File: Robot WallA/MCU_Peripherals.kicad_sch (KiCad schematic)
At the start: 44 parts, among them IC3 LAN8742A-CZ-TR, IC4 USBLC6-4SC6, IC6 USBLC6-4SC6, J3 USB4216-03-A, J6 SS-90000-009, T1 H1102NL

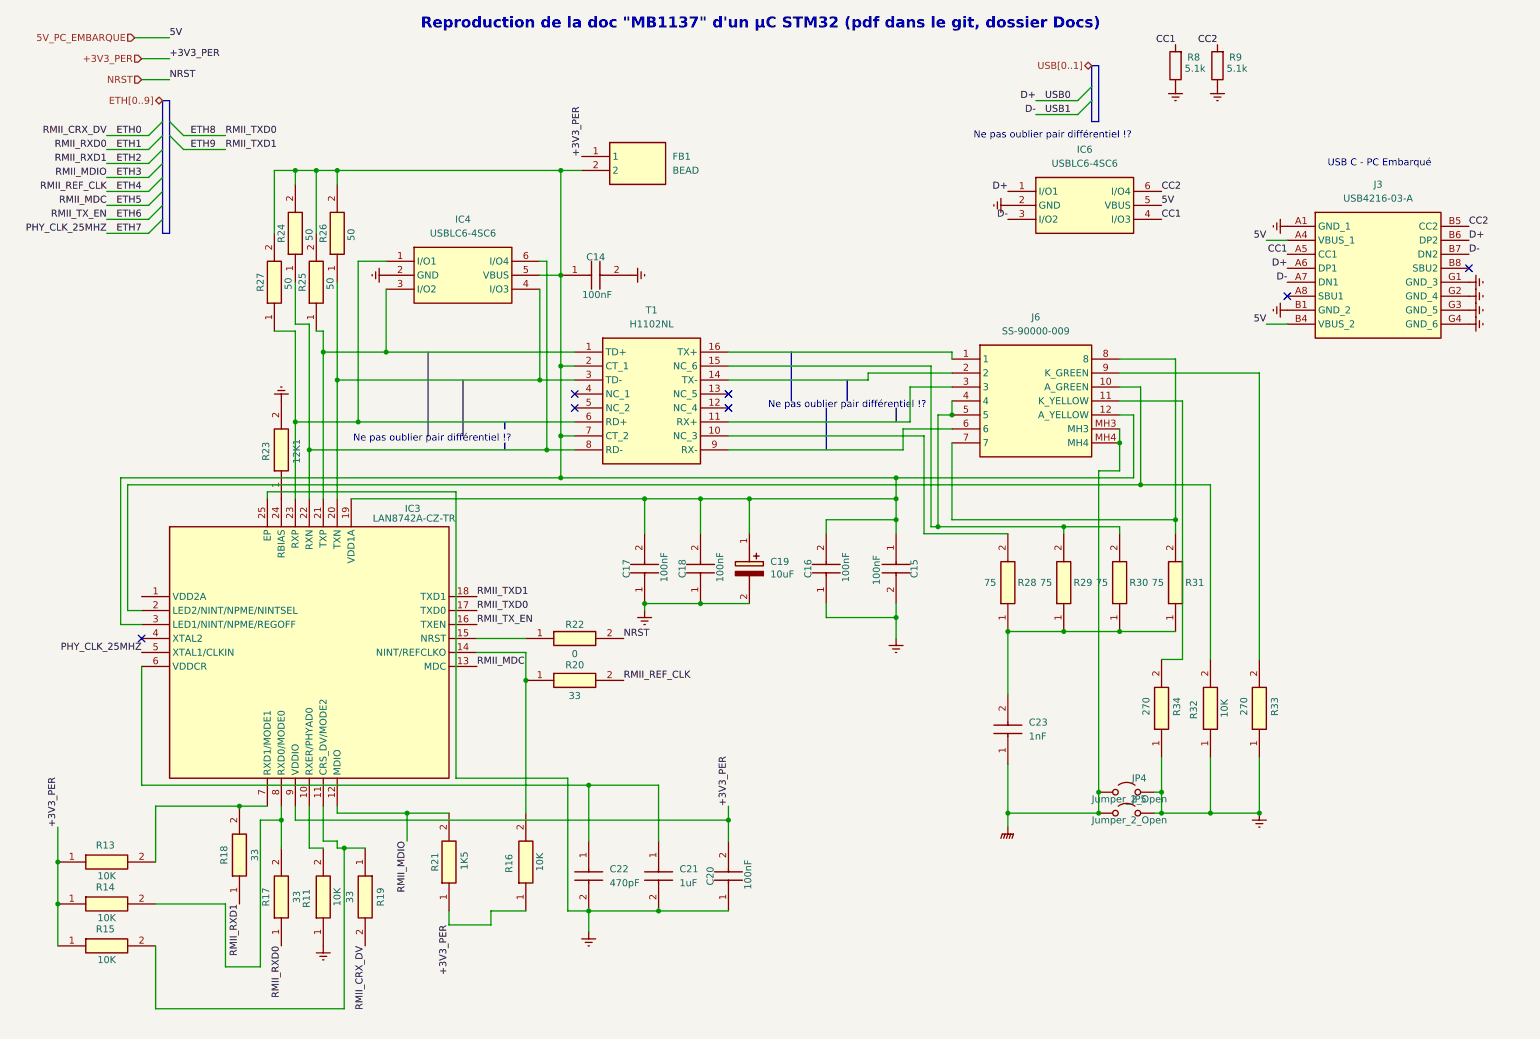
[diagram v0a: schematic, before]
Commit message: Continued to link MCU pins, Added a sheet for servomotors and optional 2 DC motors.
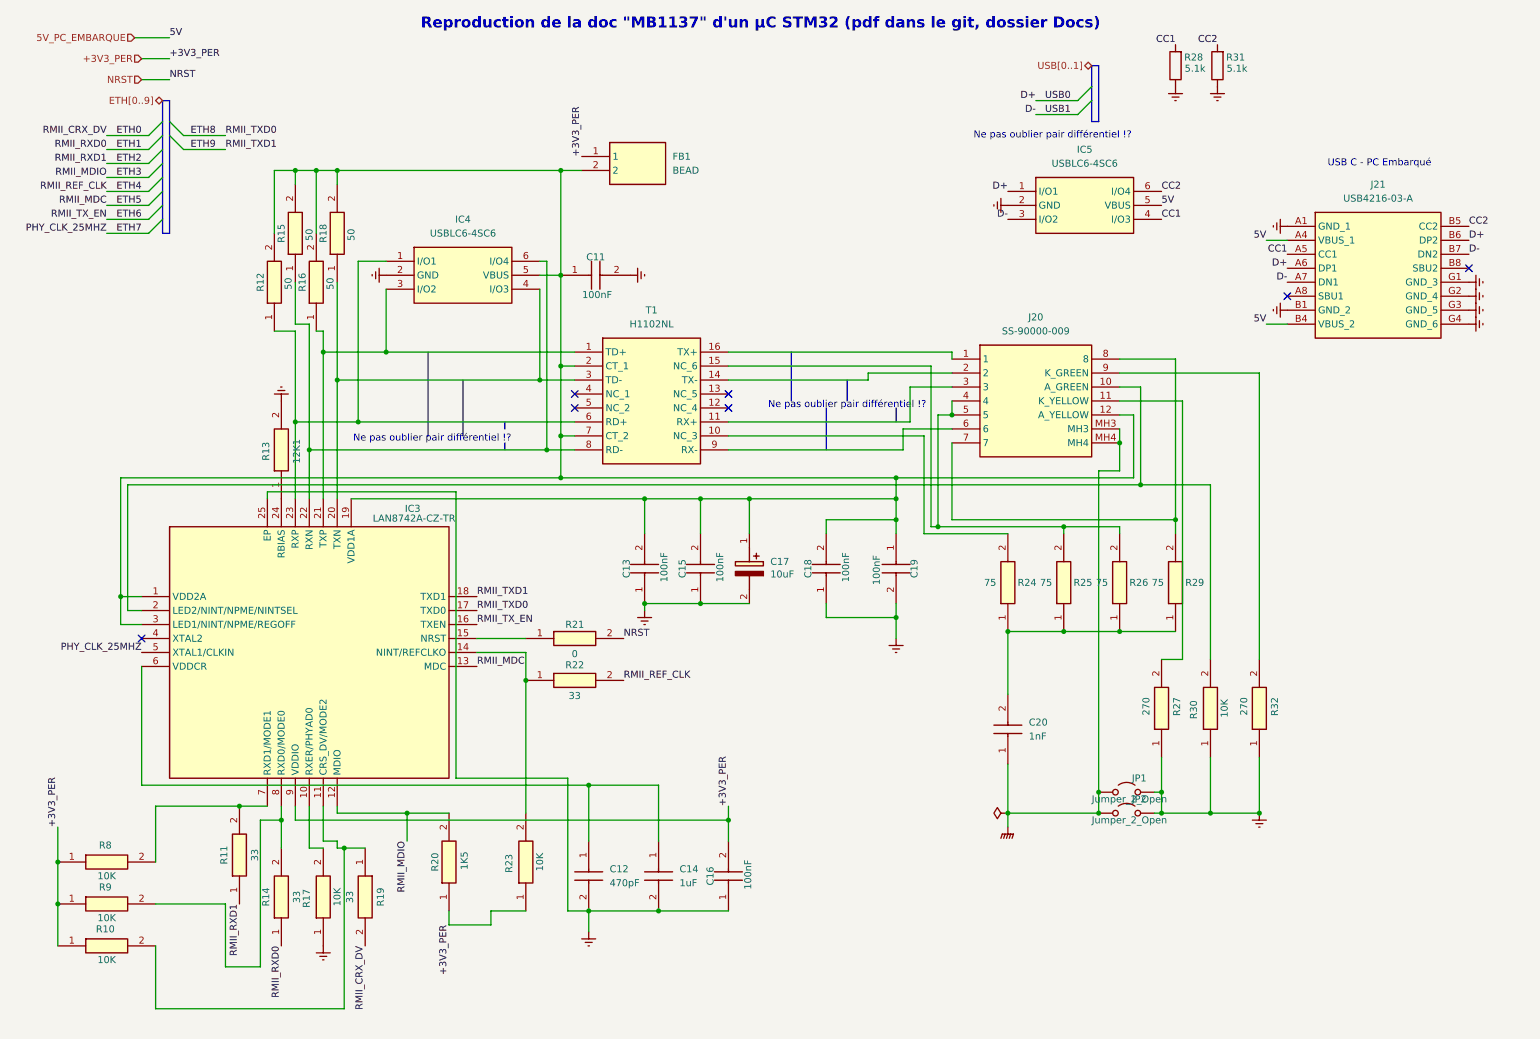
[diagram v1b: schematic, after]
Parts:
- renumbered C14 to C11, C22 to C12, C17 to C13, C21 to C14, C18 to C15, C20 to C16, C19 to C17, C16 to C18, C15 to C19, C23 to C20, IC6 to IC5, J6 to J20, J3 to J21, JP4 to JP1, JP5 to JP2, R15 to R10, R18 to R11, R27 to R12, R23 to R13, R17 to R14, R24 to R15, R25 to R16, R11 to R17, R26 to R18, R21 to R20, R22 to R21, R20 to R22, R16 to R23, R28 to R24, R29 to R25, R30 to R26, R34 to R27, R8 to R28, R31 to R29, R32 to R30, R9 to R31, R33 to R32, R13 to R8, R14 to R9
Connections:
- net at C11.1, C13.2, C15.2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: now also IC3.1 (VDD2A)

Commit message: Defined every footprints
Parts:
- C23: renamed from C11; footprint CAPC1608X90N -> Capacitor_SMD:C_0603_1608Metric_Pad1.08x0.95mm_HandSolder; Arrow Part Number CC0603KRX7R7BB104 -> (none); Arrow Price/Stock https://www.arrow.com/en/products/cc0603krx7r7bb104/yageo?u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 -> (none); Height 0.9 -> (none); Manufacturer_Name YAGEO -> (none); Manufacturer_Part_Number CC0603KRX7R7BB104 -> (none); Mouser Part Number 603-CC603KRX7R7BB104 -> (none); Mouser Price/Stock https://www.mouser.co.uk/ProductDetail/YAGEO/CC0603KRX7R7BB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 -> (none)
- C24: renamed from C17; footprint CAPPM3216X180N -> Capacitor_SMD:C_0603_1608Metric_Pad1.08x0.95mm_HandSolder; Height 1.8 -> (none); Manufacturer_Name Kyocera AVX -> (none); Manufacturer_Part_Number TAJA106K016R -> (none); Mouser Part Number N/A -> (none); Mouser Price/Stock https://www.mouser.co.uk/ProductDetail/KYOCERA-AVX/TAJA106K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 -> (none)
- C25: renamed from C19; footprint CAPC1608X90N -> Capacitor_SMD:C_0603_1608Metric_Pad1.08x0.95mm_HandSolder; Arrow Part Number CC0603KRX7R7BB104 -> (none); Arrow Price/Stock https://www.arrow.com/en/products/cc0603krx7r7bb104/yageo?u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 -> (none); Height 0.9 -> (none); Manufacturer_Name YAGEO -> (none); Manufacturer_Part_Number CC0603KRX7R7BB104 -> (none); Mouser Part Number 603-CC603KRX7R7BB104 -> (none); Mouser Price/Stock https://www.mouser.co.uk/ProductDetail/YAGEO/CC0603KRX7R7BB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 -> (none)
- C26: renamed from C13; footprint CAPC1608X90N -> Capacitor_SMD:C_0603_1608Metric_Pad1.08x0.95mm_HandSolder; Arrow Part Number CC0603KRX7R7BB104 -> (none); Arrow Price/Stock https://www.arrow.com/en/products/cc0603krx7r7bb104/yageo?u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 -> (none); Height 0.9 -> (none); Manufacturer_Name YAGEO -> (none); Manufacturer_Part_Number CC0603KRX7R7BB104 -> (none); Mouser Part Number 603-CC603KRX7R7BB104 -> (none); Mouser Price/Stock https://www.mouser.co.uk/ProductDetail/YAGEO/CC0603KRX7R7BB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 -> (none)
- C27: renamed from C15; footprint CAPC1608X90N -> Capacitor_SMD:C_0603_1608Metric_Pad1.08x0.95mm_HandSolder; Arrow Part Number CC0603KRX7R7BB104 -> (none); Arrow Price/Stock https://www.arrow.com/en/products/cc0603krx7r7bb104/yageo?u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 -> (none); Height 0.9 -> (none); Manufacturer_Name YAGEO -> (none); Manufacturer_Part_Number CC0603KRX7R7BB104 -> (none); Mouser Part Number 603-CC603KRX7R7BB104 -> (none); Mouser Price/Stock https://www.mouser.co.uk/ProductDetail/YAGEO/CC0603KRX7R7BB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 -> (none)
- C28: renamed from C18; footprint CAPC1608X90N -> Capacitor_SMD:C_0603_1608Metric_Pad1.08x0.95mm_HandSolder; Arrow Part Number CC0603KRX7R7BB104 -> (none); Arrow Price/Stock https://www.arrow.com/en/products/cc0603krx7r7bb104/yageo?u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 -> (none); Height 0.9 -> (none); Manufacturer_Name YAGEO -> (none); Manufacturer_Part_Number CC0603KRX7R7BB104 -> (none); Mouser Part Number 603-CC603KRX7R7BB104 -> (none); Mouser Price/Stock https://www.mouser.co.uk/ProductDetail/YAGEO/CC0603KRX7R7BB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 -> (none)
- C29: renamed from C20; footprint CAPC3216X145N -> Capacitor_SMD:C_0603_1608Metric_Pad1.08x0.95mm_HandSolder; Arrow Part Number CC1206KKX7RDBB102 -> (none); Arrow Price/Stock https://www.arrow.com/en/products/cc1206kkx7rdbb102/yageo?u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 -> (none); Height 1.45 -> (none); Manufacturer_Name YAGEO -> (none); Manufacturer_Part_Number CC1206KKX7RDBB102 -> (none); Mouser Part Number 603-CC206KKX7RDBB102 -> (none); Mouser Price/Stock https://www.mouser.co.uk/ProductDetail/YAGEO/CC1206KKX7RDBB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 -> (none)
- C30: renamed from C12; footprint CAPC1608X90N -> Capacitor_SMD:C_0603_1608Metric_Pad1.08x0.95mm_HandSolder; Height 0.9 -> (none); Manufacturer_Name YAGEO -> (none); Manufacturer_Part_Number CC0603JRNPO9BN471 -> (none); Mouser Part Number 603-C0603JRNPO9BN471 -> (none); Mouser Price/Stock https://www.mouser.co.uk/ProductDetail/YAGEO/CC0603JRNPO9BN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 -> (none)
- C31: renamed from C14; footprint CAPC1608X90N -> Capacitor_SMD:C_0603_1608Metric_Pad1.08x0.95mm_HandSolder; Arrow Part Number CC0603KRX5R7BB105 -> (none); Arrow Price/Stock https://www.arrow.com/en/products/cc0603krx5r7bb105/yageo?u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 -> (none); Height 0.9 -> (none); Manufacturer_Name YAGEO -> (none); Manufacturer_Part_Number CC0603KRX5R7BB105 -> (none); Mouser Part Number 603-CC603KRX5R7BB105 -> (none); Mouser Price/Stock https://www.mouser.co.uk/ProductDetail/YAGEO/CC0603KRX5R7BB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 -> (none)
- C32: renamed from C16; footprint CAPC1608X90N -> Capacitor_SMD:C_0603_1608Metric_Pad1.08x0.95mm_HandSolder; Arrow Part Number CC0603KRX7R7BB104 -> (none); Arrow Price/Stock https://www.arrow.com/en/products/cc0603krx7r7bb104/yageo?u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 -> (none); Height 0.9 -> (none); Manufacturer_Name YAGEO -> (none); Manufacturer_Part_Number CC0603KRX7R7BB104 -> (none); Mouser Part Number 603-CC603KRX7R7BB104 -> (none); Mouser Price/Stock https://www.mouser.co.uk/ProductDetail/YAGEO/CC0603KRX7R7BB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 -> (none)
- FB2: renamed from FB1; value BEAD -> Bead 600R; footprint BEADC1608X95N -> Resistor_SMD:R_0603_1608Metric_Pad0.98x0.95mm_HandSolder; Height 0.95 -> (none); Manufacturer_Name TAITEC -> (none); Manufacturer_Part_Number FCM1608KF-601T05 -> FCM 1608KF-601T03
- IC3: renamed from IC5; footprint SOT95P280X145-6N -> SamacSys_Parts:SOT95P280X145-6N; Arrow Part Number USBLC6-4SC6 -> (none); Arrow Price/Stock https://www.arrow.com/en/products/usblc6-4sc6/stmicroelectr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 -> (none); Height 1.45 -> (none); Manufacturer_Name STMicroelectronics -> (none); Mouser Part Number 511-USBLC6-4SC6 -> (none); Mouser Price/Stock https://www.mouser.co.uk/ProductDetail/STMicroelectronics/U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 -> (none)
- IC4: footprint SOT95P280X145-6N -> SamacSys_Parts:SOT95P280X145-6N; Arrow Part Number USBLC6-4SC6 -> (none); Arrow Price/Stock https://www.arrow.com/en/products/usblc6-4sc6/stmicroelectr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 -> (none); Height 1.45 -> (none); Manufacturer_Name STMicroelectronics -> (none); Mouser Part Number 511-USBLC6-4SC6 -> (none); Mouser Price/Stock https://www.mouser.co.uk/ProductDetail/STMicroelectronics/U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 -> (none)
- IC5: renamed from IC3; footprint QFN50P400X400X100-25N-D -> SamacSys_Parts:QFN50P400X400X100-25N-D; Arrow Part Number LAN8742A-CZ-TR -> (none); Arrow Price/Stock https://www.arrow.com/en/products/lan8742a-cz-tr/microchip-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 -> (none); Height 1 -> (none); Manufacturer_Name Microchip -> (none); Mouser Part Number 579-LAN8742A-CZ-TR -> (none); Mouser Price/Stock https://www.mouser.co.uk/ProductDetail/Microchip-Technology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 -> (none)
- J2: renamed from J21; footprint USB421603A -> SamacSys_Parts:USB421603A; Manufacturer_Name GCT (GLOBAL CONNECTOR TECHNOLOGY) -> (none); Mouser Part Number 640-USB4216-03-A -> (none); Mouser Price/Stock https://www.mouser.co.uk/ProductDetail/GCT/USB4216-03-A?qs=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 -> (none)
- J3: renamed from J20; footprint SS90000009 -> SamacSys_Parts:SS90000009; Height 13.38 -> (none); Manufacturer_Name Bel -> (none)
- JP4: renamed from JP1; value Jumper_2_Open -> SolderJumper; footprint (none) -> Jumper:SolderJumper-2_P1.3mm_Open_Pad1.0x1.5mm; now left out of the parts list
- JP5: renamed from JP2; value Jumper_2_Open -> SolderJumper; footprint (none) -> Jumper:SolderJumper-2_P1.3mm_Open_Pad1.0x1.5mm; now left out of the parts list
- R10: renamed from R25; value 75 -> 75R; footprint RESC1608X55N -> Resistor_SMD:R_0603_1608Metric_Pad0.98x0.95mm_HandSolder; Arrow Part Number RC0603FR-0775RL -> (none); Arrow Price/Stock https://www.arrow.com/en/products/rc0603fr-0775rl/yageo?reg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 -> (none); Height 0.55 -> (none); Manufacturer_Name KEMET -> (none); Manufacturer_Part_Number RC0603FR-0775RL -> (none); Mouser Part Number 603-RC0603FR-0775RL -> (none); Mouser Price/Stock https://www.mouser.co.uk/ProductDetail/YAGEO/RC0603FR-0775R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 -> (none)
- R11: renamed from R26; value 75 -> 75R; footprint RESC1608X55N -> Resistor_SMD:R_0603_1608Metric_Pad0.98x0.95mm_HandSolder; Arrow Part Number RC0603FR-0775RL -> (none); Arrow Price/Stock https://www.arrow.com/en/products/rc0603fr-0775rl/yageo?reg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 -> (none); Height 0.55 -> (none); Manufacturer_Name KEMET -> (none); Manufacturer_Part_Number RC0603FR-0775RL -> (none); Mouser Part Number 603-RC0603FR-0775RL -> (none); Mouser Price/Stock https://www.mouser.co.uk/ProductDetail/YAGEO/RC0603FR-0775R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 -> (none)
- R12: renamed from R29; value 75 -> 75R; footprint RESC1608X55N -> Resistor_SMD:R_0603_1608Metric_Pad0.98x0.95mm_HandSolder; Arrow Part Number RC0603FR-0775RL -> (none); Arrow Price/Stock https://www.arrow.com/en/products/rc0603fr-0775rl/yageo?reg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 -> (none); Height 0.55 -> (none); Manufacturer_Name KEMET -> (none); Manufacturer_Part_Number RC0603FR-0775RL -> (none); Mouser Part Number 603-RC0603FR-0775RL -> (none); Mouser Price/Stock https://www.mouser.co.uk/ProductDetail/YAGEO/RC0603FR-0775R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 -> (none)
- R13: renamed from R21; value 0 -> 0R; footprint RESC1608X50N -> Resistor_SMD:R_0603_1608Metric_Pad0.98x0.95mm_HandSolder; Arrow Part Number CRCW06030000Z0EI -> (none); Arrow Price/Stock https://www.arrow.com/en/products/crcw06030000z0ei/vishay?u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 -> (none); Height 0.5 -> (none); Manufacturer_Name Vishay -> (none); Manufacturer_Part_Number CRCW06030000Z0EI -> (none); Mouser Part Number 71-CRCW06030000Z0EI -> (none); Mouser Price/Stock https://www.mouser.co.uk/ProductDetail/Vishay-Dale/CRCW0603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 -> (none)
- R14: renamed from R22; value 33 -> 33R; footprint RESC1608X55N -> Resistor_SMD:R_0603_1608Metric_Pad0.98x0.95mm_HandSolder; Height 0.55 -> (none); Manufacturer_Name TE Connectivity -> (none); Manufacturer_Part_Number CRG0603F33R -> (none); Mouser Part Number 279-CRG0603F33R -> (none); Mouser Price/Stock https://www.mouser.co.uk/ProductDetail/TE-Connectivity-Hols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 -> (none)
- R15: renamed from R27; value 270 -> 270R; footprint RESC1608X55N -> Resistor_SMD:R_0603_1608Metric_Pad0.98x0.95mm_HandSolder; Arrow Part Number RC0603FR-07270RL -> (none); Arrow Price/Stock https://www.arrow.com/en/products/rc0603fr-07270rl/yageo?re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 -> (none); Height 0.55 -> (none); Manufacturer_Name KEMET -> (none); Manufacturer_Part_Number RC0603FR-07270RL -> (none); Mouser Part Number 603-RC0603FR-07270RL -> (none); Mouser Price/Stock https://www.mouser.co.uk/ProductDetail/Yageo/RC0603FR-07270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 -> (none)
- R16: renamed from R30; footprint RESC1608X50N -> Resistor_SMD:R_0603_1608Metric_Pad0.98x0.95mm_HandSolder; Arrow Part Number CRCW060310K0FKEI -> (none); Arrow Price/Stock https://www.arrow.com/en/products/crcw060310k0fkei/vishay?u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 -> (none); Height 0.5 -> (none); Manufacturer_Name Vishay -> (none); Manufacturer_Part_Number CRCW060310K0FKEI -> (none); Mouser Part Number 71-CRCW060310K0FKEI -> (none); Mouser Price/Stock https://www.mouser.co.uk/ProductDetail/Vishay-Dale/CRCW0603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 -> (none)
- R17: renamed from R32; value 270 -> 270R; footprint RESC1608X55N -> Resistor_SMD:R_0603_1608Metric_Pad0.98x0.95mm_HandSolder; Arrow Part Number RC0603FR-07270RL -> (none); Arrow Price/Stock https://www.arrow.com/en/products/rc0603fr-07270rl/yageo?re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 -> (none); Height 0.55 -> (none); Manufacturer_Name KEMET -> (none); Manufacturer_Part_Number RC0603FR-07270RL -> (none); Mouser Part Number 603-RC0603FR-07270RL -> (none); Mouser Price/Stock https://www.mouser.co.uk/ProductDetail/Yageo/RC0603FR-07270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 -> (none)
- R18: renamed from R19; value 33 -> 33R; footprint RESC1608X55N -> Resistor_SMD:R_0603_1608Metric_Pad0.98x0.95mm_HandSolder; Height 0.55 -> (none); Manufacturer_Name TE Connectivity -> (none); Manufacturer_Part_Number CRG0603F33R -> (none); Mouser Part Number 279-CRG0603F33R -> (none); Mouser Price/Stock https://www.mouser.co.uk/ProductDetail/TE-Connectivity-Hols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 -> (none)
- R19: renamed from R8; footprint RESC1608X50N -> Resistor_SMD:R_0603_1608Metric_Pad0.98x0.95mm_HandSolder; Arrow Part Number CRCW060310K0FKEI -> (none); Arrow Price/Stock https://www.arrow.com/en/products/crcw060310k0fkei/vishay?u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 -> (none); Height 0.5 -> (none); Manufacturer_Name Vishay -> (none); Manufacturer_Part_Number CRCW060310K0FKEI -> (none); Mouser Part Number 71-CRCW060310K0FKEI -> (none); Mouser Price/Stock https://www.mouser.co.uk/ProductDetail/Vishay-Dale/CRCW0603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 -> (none)
- R2: renamed from R28; footprint (none) -> Resistor_SMD:R_0603_1608Metric_Pad0.98x0.95mm_HandSolder
- R20: renamed from R9; footprint RESC1608X50N -> Resistor_SMD:R_0603_1608Metric_Pad0.98x0.95mm_HandSolder; Arrow Part Number CRCW060310K0FKEI -> (none); Arrow Price/Stock https://www.arrow.com/en/products/crcw060310k0fkei/vishay?u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 -> (none); Height 0.5 -> (none); Manufacturer_Name Vishay -> (none); Manufacturer_Part_Number CRCW060310K0FKEI -> (none); Mouser Part Number 71-CRCW060310K0FKEI -> (none); Mouser Price/Stock https://www.mouser.co.uk/ProductDetail/Vishay-Dale/CRCW0603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 -> (none)
- R21: renamed from R11; value 33 -> 33R; footprint RESC1608X55N -> Resistor_SMD:R_0603_1608Metric_Pad0.98x0.95mm_HandSolder; Height 0.55 -> (none); Manufacturer_Name TE Connectivity -> (none); Manufacturer_Part_Number CRG0603F33R -> (none); Mouser Part Number 279-CRG0603F33R -> (none); Mouser Price/Stock https://www.mouser.co.uk/ProductDetail/TE-Connectivity-Hols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 -> (none)
- R22: renamed from R20; value 1K5 -> 1.5k; footprint RESC1608X50N -> Resistor_SMD:R_0603_1608Metric_Pad0.98x0.95mm_HandSolder; Arrow Part Number CRCW06031K50FKED -> (none); Arrow Price/Stock https://www.arrow.com/en/products/crcw06031k50fked/vishay?r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 -> (none); Height 0.5 -> (none); Manufacturer_Name Vishay -> (none); Manufacturer_Part_Number CRCW06031K50FKED -> (none)
- R23: footprint RESC1608X50N -> Resistor_SMD:R_0603_1608Metric_Pad0.98x0.95mm_HandSolder; Arrow Part Number CRCW060310K0FKEI -> (none); Arrow Price/Stock https://www.arrow.com/en/products/crcw060310k0fkei/vishay?u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 -> (none); Height 0.5 -> (none); Manufacturer_Name Vishay -> (none); Manufacturer_Part_Number CRCW060310K0FKEI -> (none); Mouser Part Number 71-CRCW060310K0FKEI -> (none); Mouser Price/Stock https://www.mouser.co.uk/ProductDetail/Vishay-Dale/CRCW0603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 -> (none)
- R24: renamed from R10; footprint RESC1608X50N -> Resistor_SMD:R_0603_1608Metric_Pad0.98x0.95mm_HandSolder; Arrow Part Number CRCW060310K0FKEI -> (none); Arrow Price/Stock https://www.arrow.com/en/products/crcw060310k0fkei/vishay?u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 -> (none); Height 0.5 -> (none); Manufacturer_Name Vishay -> (none); Manufacturer_Part_Number CRCW060310K0FKEI -> (none); Mouser Part Number 71-CRCW060310K0FKEI -> (none); Mouser Price/Stock https://www.mouser.co.uk/ProductDetail/Vishay-Dale/CRCW0603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 -> (none)
- R25: renamed from R14; value 33 -> 33R; footprint RESC1608X55N -> Resistor_SMD:R_0603_1608Metric_Pad0.98x0.95mm_HandSolder; Height 0.55 -> (none); Manufacturer_Name TE Connectivity -> (none); Manufacturer_Part_Number CRG0603F33R -> (none); Mouser Part Number 279-CRG0603F33R -> (none); Mouser Price/Stock https://www.mouser.co.uk/ProductDetail/TE-Connectivity-Hols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 -> (none)
- R26: renamed from R17; footprint RESC1608X50N -> Resistor_SMD:R_0603_1608Metric_Pad0.98x0.95mm_HandSolder; Arrow Part Number CRCW060310K0FKEI -> (none); Arrow Price/Stock https://www.arrow.com/en/products/crcw060310k0fkei/vishay?u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 -> (none); Height 0.5 -> (none); Manufacturer_Name Vishay -> (none); Manufacturer_Part_Number CRCW060310K0FKEI -> (none); Mouser Part Number 71-CRCW060310K0FKEI -> (none); Mouser Price/Stock https://www.mouser.co.uk/ProductDetail/Vishay-Dale/CRCW0603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 -> (none)
- R3: renamed from R31; footprint (none) -> Resistor_SMD:R_0603_1608Metric_Pad0.98x0.95mm_HandSolder
- R4: renamed from R15; value 50 -> 50R; footprint RESC1608X55N -> Resistor_SMD:R_0603_1608Metric_Pad0.98x0.95mm_HandSolder; Height 0.55 -> (none); Manufacturer_Name Vishay -> (none); Manufacturer_Part_Number TNPW060350R0DEEA -> (none); Mouser Part Number 71-TNPW060350R0DEEA -> (none); Mouser Price/Stock https://www.mouser.co.uk/ProductDetail/Vishay-Dale/TNPW0603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 -> (none)
- R5: renamed from R18; value 50 -> 50R; footprint RESC1608X55N -> Resistor_SMD:R_0603_1608Metric_Pad0.98x0.95mm_HandSolder; Height 0.55 -> (none); Manufacturer_Name Vishay -> (none); Manufacturer_Part_Number TNPW060350R0DEEA -> (none); Mouser Part Number 71-TNPW060350R0DEEA -> (none); Mouser Price/Stock https://www.mouser.co.uk/ProductDetail/Vishay-Dale/TNPW0603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 -> (none)
- R6: renamed from R12; value 50 -> 50R; footprint RESC1608X55N -> Resistor_SMD:R_0603_1608Metric_Pad0.98x0.95mm_HandSolder; Height 0.55 -> (none); Manufacturer_Name Vishay -> (none); Manufacturer_Part_Number TNPW060350R0DEEA -> (none); Mouser Part Number 71-TNPW060350R0DEEA -> (none); Mouser Price/Stock https://www.mouser.co.uk/ProductDetail/Vishay-Dale/TNPW0603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 -> (none)
- R7: renamed from R16; value 50 -> 50R; footprint RESC1608X55N -> Resistor_SMD:R_0603_1608Metric_Pad0.98x0.95mm_HandSolder; Height 0.55 -> (none); Manufacturer_Name Vishay -> (none); Manufacturer_Part_Number TNPW060350R0DEEA -> (none); Mouser Part Number 71-TNPW060350R0DEEA -> (none); Mouser Price/Stock https://www.mouser.co.uk/ProductDetail/Vishay-Dale/TNPW0603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 -> (none)
- R8: renamed from R13; value 12K1 -> 12.1k; footprint RESC1609X55N -> Resistor_SMD:R_0603_1608Metric_Pad0.98x0.95mm_HandSolder; Height 0.55 -> (none); Manufacturer_Name Panasonic -> (none); Manufacturer_Part_Number ERJ-P03F1212V -> (none); Mouser Part Number 667-ERJ-P03F1212V -> (none); Mouser Price/Stock https://www.mouser.co.uk/ProductDetail/Panasonic/ERJ-P03F12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 -> (none)
- R9: renamed from R24; value 75 -> 75R; footprint RESC1608X55N -> Resistor_SMD:R_0603_1608Metric_Pad0.98x0.95mm_HandSolder; Arrow Part Number RC0603FR-0775RL -> (none); Arrow Price/Stock https://www.arrow.com/en/products/rc0603fr-0775rl/yageo?reg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 -> (none); Height 0.55 -> (none); Manufacturer_Name KEMET -> (none); Manufacturer_Part_Number RC0603FR-0775RL -> (none); Mouser Part Number 603-RC0603FR-0775RL -> (none); Mouser Price/Stock https://www.mouser.co.uk/ProductDetail/YAGEO/RC0603FR-0775R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 -> (none)
- T1: footprint SOIC127P940X597-16N -> SamacSys_Parts:SOIC127P940X597-16N; Arrow Part Number H1102NL -> (none); Arrow Price/Stock https://www.arrow.com/en/products/h1102nl/pulse-electronics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 -> (none); Height 5.97 -> (none); Manufacturer_Name PULSE -> (none); Mouser Part Number 673-H1102NL -> (none); Mouser Price/Stock https://www.mouser.co.uk/ProductDetail/Pulse-Electronics/H1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 -> (none)
